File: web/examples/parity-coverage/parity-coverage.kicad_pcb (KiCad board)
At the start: 2 copper layers, 40 x 30 mm, 1 part

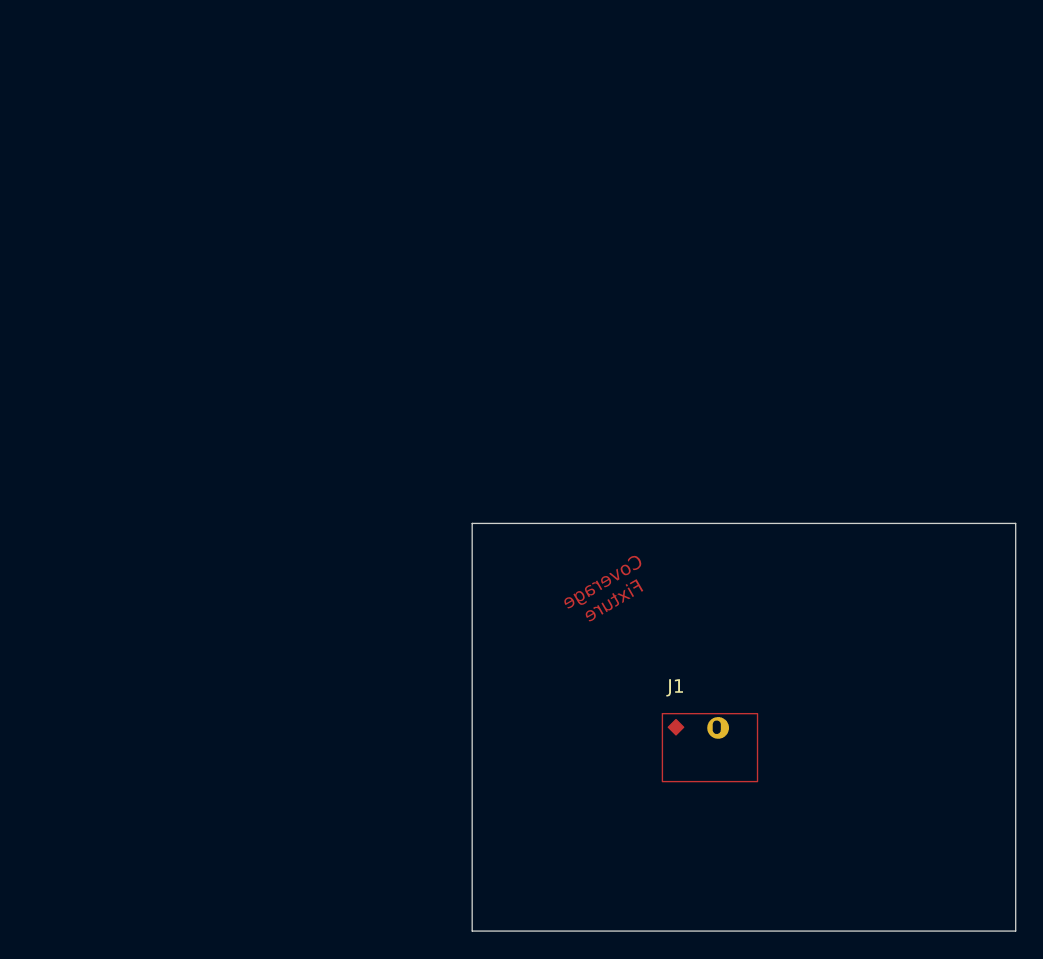
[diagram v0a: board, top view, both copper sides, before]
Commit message: Port copper-graphics-as-obstacles to the JS KiCad adapter
Mirrors the Rust port: fp_line/fp_circle/fp_arc/fp_poly/fp_text inside
footprints, and gr_line/gr_circle/gr_arc/gr_poly/gr_rect at board
level, become fixed obstacles via a shared boundingBox helper and a
textRectangle extracted from the existing gr_text handling. gr_curve
and fp_curve still throw.

Extends the parity-coverage fixture with all ten new kinds, including
a footprint at a non-zero rotation, so kicad_pcb_parity.rs exercises
the new code paths against the Rust port.

Co-Authored-By: Claude Sonnet 5 <noreply@anthropic.com>
Claude-Session: https://claude.ai/code/session_01Q47EhgqP74pEnxWoUrbvJi
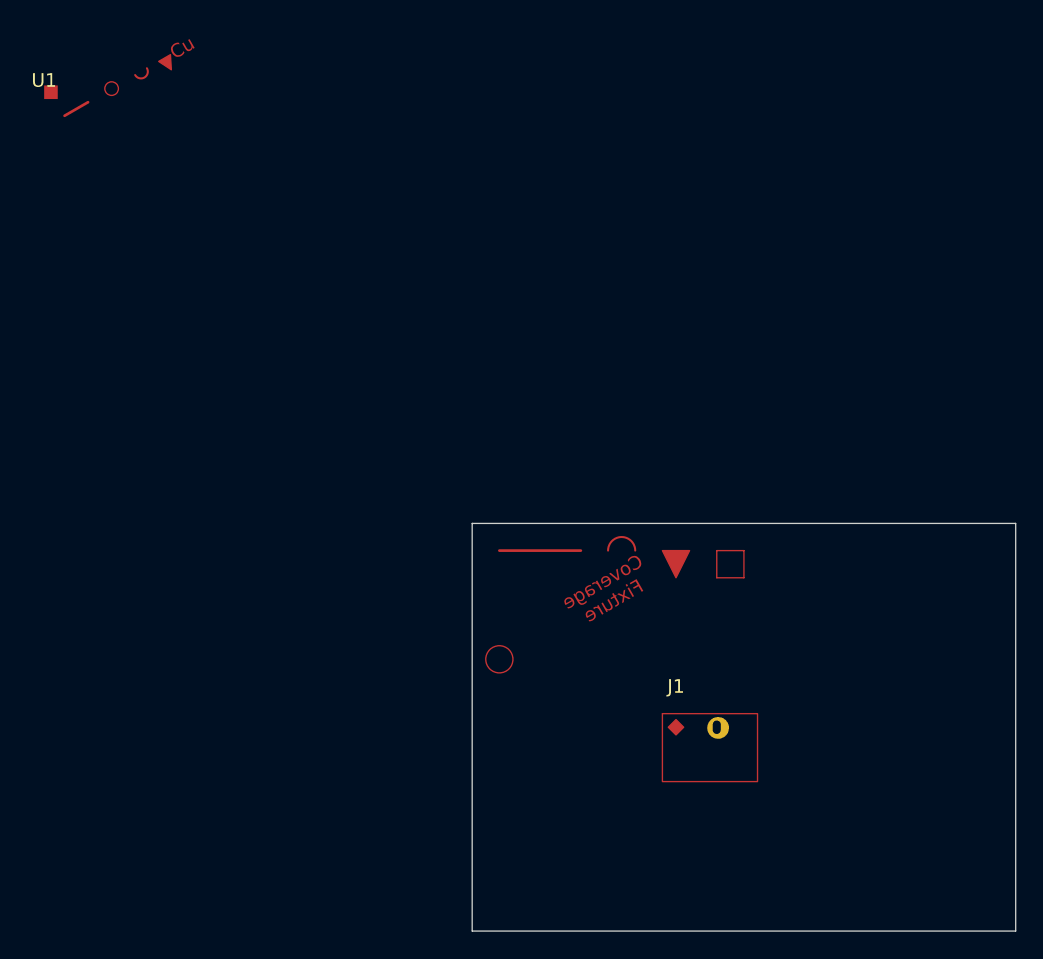
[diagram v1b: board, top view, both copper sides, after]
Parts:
- added U1: , Coverage:CopperGraphics, F.Cu at (60.0, 60.0)
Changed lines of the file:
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@@
       (net 1 "Signal"))
     (pad "2" thru_hole circle (at 3 0) (size 1.6 1.6) (drill oval 0.6 1.0 (offset 0.1 0.05)) (layers "*.Cu" "*.Mask") (net 2 "Return")))
+  (footprint "Coverage:CopperGraphics" (layer "F.Cu") (at 60 60 30)
+    (property "Reference" "U1" (at 0 -3) (layer "F.SilkS") (effects (font (size 1 1) (thickness 0.15))))
+    (fp_line (start 0 0) (end 2 0) (layer "F.Cu") (stroke (width 0.2) (type solid)))
+    (fp_circle (center 4 0) (end 4.5 0) (layer "F.Cu") (stroke (width 0.1) (type solid)) (fill none))
+    (fp_arc (start 6 0) (mid 6.5 0.5) (end 7 0) (layer "F.Cu") (stroke (width 0.15) (type solid)))
+    (fp_poly (pts (xy 8 0) (xy 9 0) (xy 8.5 1)) (layer "F.Cu") (stroke (width 0.1) (type solid)) (fill yes))
+    (fp_text user "Cu" (at 10 0 30) (layer "F.Cu") (effects (font (size 1 1) (thickness 0.15))))
+    (pad "1" smd rect (at 0 -2) (size 1 1) (layers "F.Cu") (net 1 "Signal")))
+  (gr_line (start 92 92) (end 98 92) (layer "F.Cu") (stroke (width 0.2) (type solid)))
+  (gr_circle (center 92 100) (end 92 101) (layer "F.Cu") (stroke (width 0.1) (type solid)) (fill none))
+  (gr_arc (start 100 92) (mid 101 91) (end 102 92) (layer "F.Cu") (stroke (width 0.15) (type solid)))
+  (gr_poly (pts (xy 104 92) (xy 106 92) (xy 105 94)) (layer "F.Cu") (stroke (width 0.1) (type solid)) (fill yes))
+  (gr_rect (start 108 92) (end 110 94) (layer "F.Cu") (stroke (width 0.1) (type solid)) (fill none))
   (gr_rect (start 90 90) (end 130 120) (stroke (width 0.05) (type default)) (fill none) (layer "Edge.Cuts")))

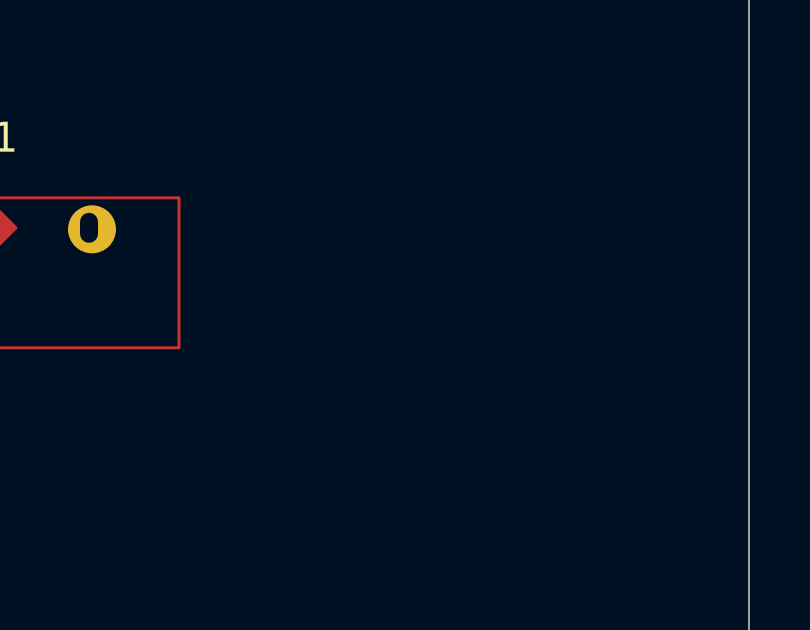
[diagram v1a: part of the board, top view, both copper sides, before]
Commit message: Build custom pad copper from every primitive and the anchor
The pad outline was already a convex hull over stroke-inflated sample
points; this widens the sample set rather than replacing the machinery.
Every primitive kind contributes (poly, line, rect, arc, circle), and the
anchor joins them when the primitives do not already cover it, so a pad
whose outline covers its anchor keeps the polygon it had.

A circular anchor takes its diameter from size.x alone and a rectangular
one is the whole size box, both checked against KiCad 10.0.3. Pads that
are not a single convex filled outline now warn that the hull can
overstate their copper.

Co-Authored-By: Claude Opus 5 (1M context) <noreply@anthropic.com>
Claude-Session: https://claude.ai/code/session_01Q47EhgqP74pEnxWoUrbvJi
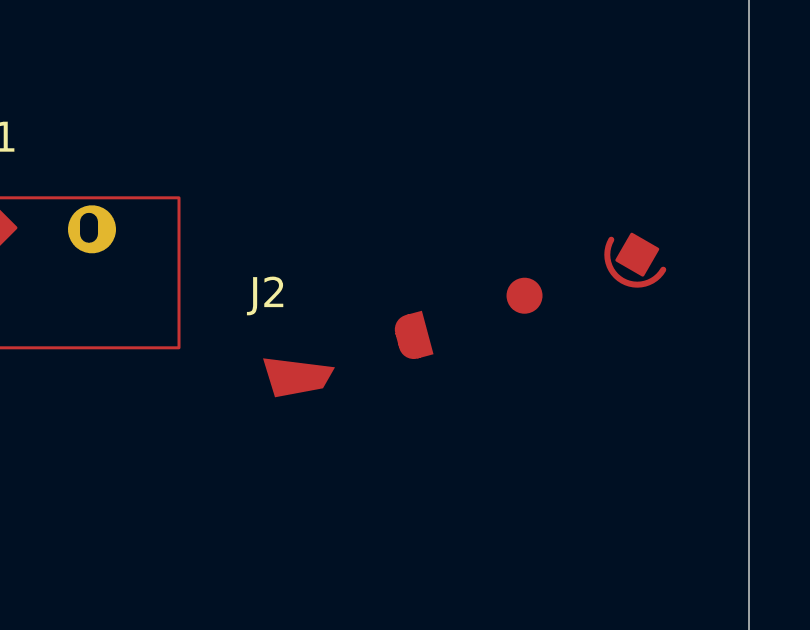
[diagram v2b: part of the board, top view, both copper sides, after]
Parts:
- added J2: , Coverage:PadShapes, F.Cu at (115.0, 110.0)
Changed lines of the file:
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@@
   (gr_poly (pts (xy 104 92) (xy 106 92) (xy 105 94)) (layer "F.Cu") (stroke (width 0.1) (type solid)) (fill yes))
   (gr_rect (start 108 92) (end 110 94) (layer "F.Cu") (stroke (width 0.1) (type solid)) (fill none))
+  (footprint "Coverage:PadShapes" (layer "F.Cu") (at 115 110 20)
+    (property "Reference" "J2" (at 0 -3) (layer "F.SilkS") (effects (font (size 1 1) (thickness 0.15))))
+    (pad "1" smd trapezoid (at 0 0) (size 2 1) (rect_delta 0.3 -0.4) (layers "F.Cu") (net 1 "Signal"))
+    (pad "2" smd custom (at 4 0 15) (size 1 0.5) (layers "F.Cu")
+      (options (clearance outline) (anchor rect))
+      (primitives
+        (gr_poly (pts (xy 0.55 0.75) (xy 0 0.75) (xy 0 -0.75) (xy 0.55 -0.75)) (width 0))
+        (gr_circle (center 0 -0.25) (end 0.5 -0.25) (width 0))
+        (gr_circle (center 0 0.25) (end 0.5 0.25) (width 0))
+      )
+      (net 2 "Return"))
+    (pad "3" smd custom (at 8 0) (size 1.2 0.4) (layers "F.Cu")
+      (options (clearance outline) (anchor circle))
+      (primitives
+        (gr_line (start -0.1 0) (end 0.1 0) (width 0.1))
+        (gr_line (start 0 -0.1) (end 0 0.1) (width 0.1))
+      )
+      (net 1 "Signal"))
+    (pad "4" smd custom (at 12 0 -30) (size 0.5 0.5) (layers "F.Cu")
+      (options (clearance outline) (anchor circle))
+      (primitives
+        (gr_arc (start -1 0) (mid 0 1) (end 1 0) (width 0.2))
+        (gr_rect (start -0.5 -0.5) (end 0.5 0.5) (width 0.1) (fill yes))
+      )
+      (net 2 "Return")))
   (gr_rect (start 90 90) (end 130 120) (stroke (width 0.05) (type default)) (fill none) (layer "Edge.Cuts")))
